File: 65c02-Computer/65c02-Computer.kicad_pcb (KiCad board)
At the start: 2 copper layers, 16 parts, among them SW1 SW_Push, U1 65C02, U2 62C256, U3 74LS04, U4 28C256, U5 LM555, X1 MXO-45HST

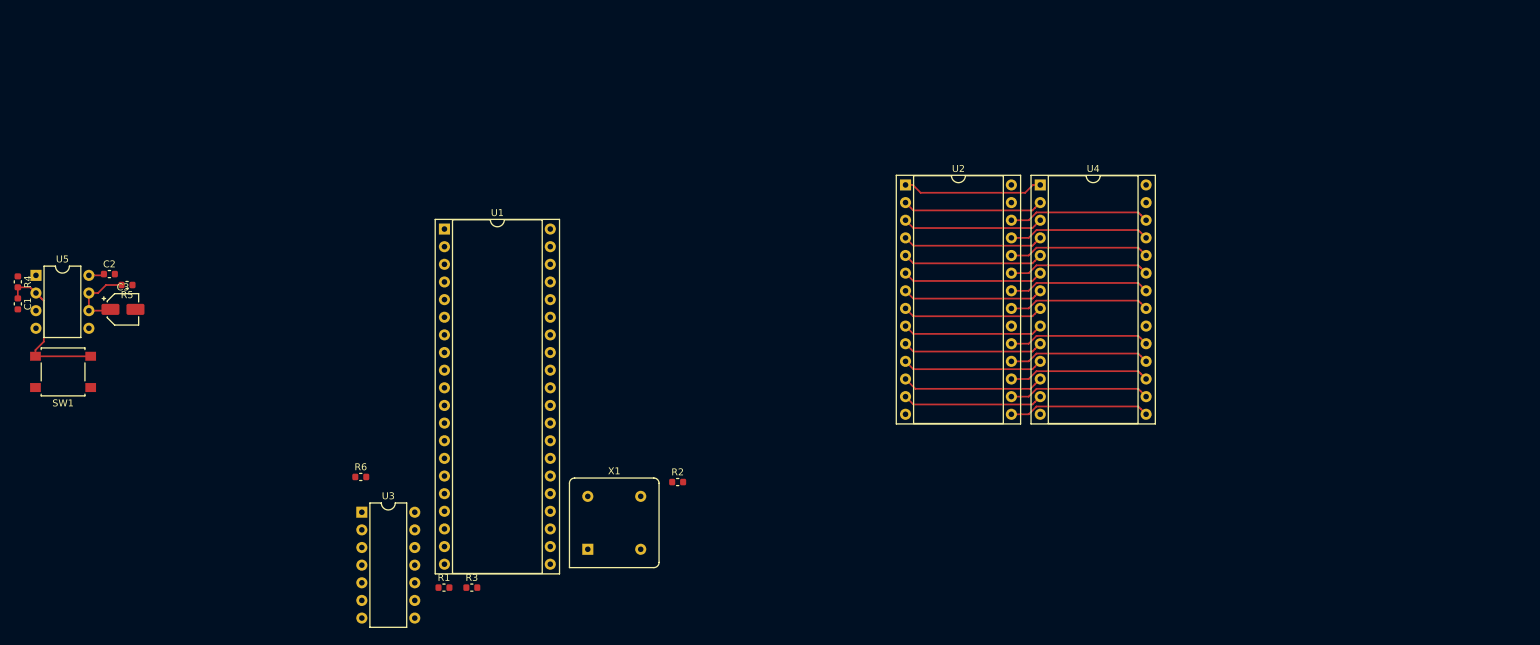
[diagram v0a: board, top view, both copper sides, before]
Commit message: Update pcb and put arduino sketch
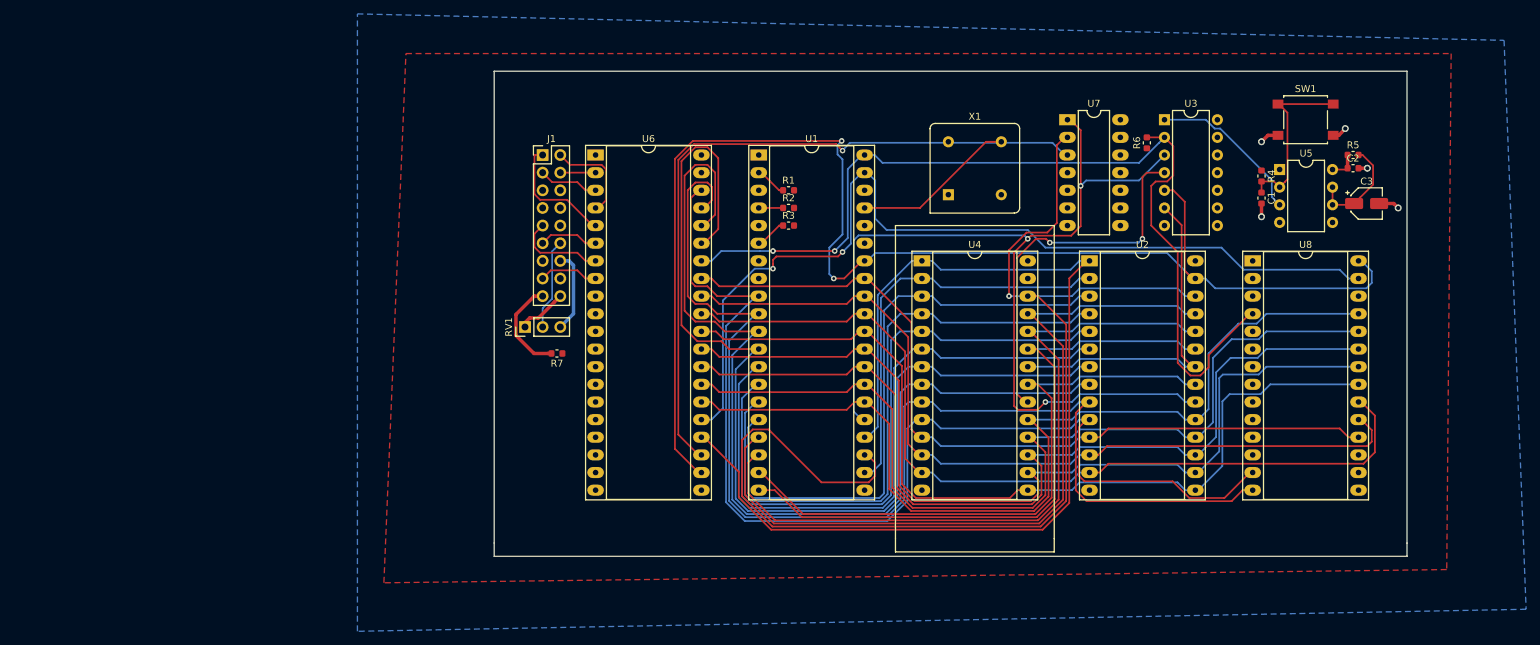
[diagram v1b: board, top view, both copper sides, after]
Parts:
- added J1: Conn_02x09_Odd_Even, Connector_PinHeader_2.54mm:PinHeader_2x09_P2.54mm_Vertical, F.Cu at (112.4, 38.1)
- added R7: 150, Resistor_SMD:R_0603_1608Metric, F.Cu at (114.5, 66.7)
- added RV1: 10k, Connector_PinHeader_2.54mm:PinHeader_1x03_P2.54mm_Vertical, F.Cu at (109.9, 62.9)
- added U6: 65C22, Package_DIP:DIP-40_W15.24mm_Socket_LongPads, F.Cu at (120.0, 38.1)
- added U7: 74LS32, Package_DIP:DIP-14_W7.62mm_LongPads, F.Cu at (188.0, 33.0)
- added U8: 65C51S, Package_DIP:DIP-28_W15.24mm_Socket_LongPads, F.Cu at (214.6, 53.3)
- U1: footprint Package_DIP:DIP-40_W15.24mm_Socket -> Package_DIP:DIP-40_W15.24mm_Socket_LongPads
- U2, U4: footprint Package_DIP:DIP-28_W15.24mm_Socket -> Package_DIP:DIP-28_W15.24mm_Socket_LongPads
- moved SW1 182.6 mm to (222.2, 33.0)
- moved C1 179.7 mm to (215.9, 44.3)
- moved C2 179.7 mm to (229.1, 40.0)
- moved C3 179.7 mm to (231.0, 45.1)
- moved R4 179.7 mm to (215.9, 41.1)
- moved U5 179.7 mm to (218.5, 40.2)
- moved R5 177.5 mm to (229.1, 38.1), turned to 0 degrees
- moved U3 128.6 mm to (201.9, 33.0)
- moved R6 123.0 mm to (199.4, 36.3), turned to 90 degrees
- moved R1 75.7 mm to (147.8, 43.2)
- moved X1 72.8 mm to (170.8, 43.8)
- moved R3 69.3 mm to (147.8, 48.3)
- moved U1 46.5 mm to (143.5, 38.1)
- moved R2 42.6 mm to (147.8, 45.7)
- moved U2 28.7 mm to (191.1, 53.3)
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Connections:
- net /Reset/~RESET renamed /~RESET
- net Net-(U1-Pad37) renamed /CLK
- U1 pad 39: (no net) -> /PHI2
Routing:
- net ~WR: track 0.00 -> 194.6 mm, vias 0 -> 2
- net /A13: track 20.3 -> 174.0 mm, vias 0 -> 1
- net /A1: track 20.3 -> 173.4 mm
- net /A15: track 0.00 -> 143.5 mm, vias 0 -> 3
- net /A0: track 20.3 -> 160.7 mm
- net /~RESET: track 0.00 -> 136.5 mm, vias 0 -> 2
- net /PHI2: track 0.00 -> 134.2 mm, vias 0 -> 2
- net /A14: track 20.3 -> 154.0 mm
- net /A3: track 20.3 -> 151.7 mm
- net /A2: track 20.3 -> 142.3 mm
- net /D7: track 20.3 -> 135.9 mm
- net /D6: track 20.3 -> 135.1 mm
- net /D5: track 20.3 -> 133.5 mm
- net /D4: track 20.3 -> 132.7 mm
- net /D3: track 20.3 -> 128.6 mm
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- added copper zone on F.Cu, net +5V
- added copper zone on B.Cu, net GND
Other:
- board outline added: 131.4 x 69.9 mm
- net class Power added: clearance 0.2, trace_width 0.5, via_dia 1, via_drill 0.6

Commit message: Create v2
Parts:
- removed the C2 at (229.1, 40.0)
- removed the R4 at (215.9, 41.1)
- removed the U5 at (218.5, 40.2)
- added C1: 27p, Capacitor_THT:C_Disc_D3.8mm_W2.6mm_P2.50mm, F.Cu at (213.4, 85.7)
- added C4: 10u, Capacitor_THT:CP_Radial_D8.0mm_P5.00mm, F.Cu at (231.0, 46.4)
- added J1: Barrel_Jack, Connector_BarrelJack:BarrelJack_CUI_PJ-102AH_Horizontal, F.Cu at (259.7, 41.3)
- added J2: Conn_01x06, Connector_PinSocket_2.54mm:PinSocket_1x06_P2.54mm_Horizontal, F.Cu at (250.2, 37.5)
- added J4: Conn_01x02, Connector_PinHeader_2.54mm:PinHeader_1x02_P2.54mm_Vertical, F.Cu at (229.2, 31.1)
- added R6: 30k, Resistor_THT:R_Axial_DIN0207_L6.3mm_D2.5mm_P10.16mm_Horizontal, F.Cu at (233.0, 30.5)
- added U10: 74LS138, Package_DIP:DIP-16_W7.62mm_LongPads, F.Cu at (189.2, 30.5)
- added U6: 65C22, Package_DIP:DIP-40_W15.24mm_Socket_LongPads, F.Cu at (89.5, 38.1)
- added U9: 74LS30, Package_DIP:DIP-14_W7.62mm_LongPads, F.Cu at (210.8, 53.3)
- added Y1: 1.8432MHz, Crystal:Crystal_HC49-U_Vertical, F.Cu at (214.6, 79.4)
- C2: renamed from C1; footprint Capacitor_SMD:C_0603_1608Metric -> Capacitor_THT:C_Disc_D3.8mm_W2.6mm_P2.50mm
- C3: value 10u -> C; footprint Capacitor_SMD:CP_Elec_4x3 -> Capacitor_THT:C_Disc_D3.8mm_W2.6mm_P2.50mm
- R1, R2, R3: footprint Resistor_SMD:R_0603_1608Metric -> Resistor_THT:R_Axial_DIN0207_L6.3mm_D2.5mm_P10.16mm_Horizontal
- R4: renamed from R7; footprint Resistor_SMD:R_0603_1608Metric -> Resistor_THT:R_Axial_DIN0207_L6.3mm_D2.5mm_P10.16mm_Horizontal
- R5: value 30k -> 1M; footprint Resistor_SMD:R_0603_1608Metric -> Resistor_THT:R_Axial_DIN0207_L6.3mm_D2.5mm_P10.16mm_Horizontal
- R7: renamed from R6; footprint Resistor_SMD:R_0603_1608Metric -> Resistor_THT:R_Axial_DIN0207_L6.3mm_D2.5mm_P10.16mm_Horizontal
- SW1: footprint Button_Switch_SMD:SW_SPST_B3S-1000 -> Button_Switch_THT:SW_PUSH_6mm_H4.3mm
- U7: value 74LS32 -> LM555; footprint Package_DIP:DIP-14_W7.62mm_LongPads -> Package_DIP:DIP-8_W7.62mm
- moved U7 31.4 mm to (218.5, 40.2)
- moved R5 16.4 mm to (215.3, 29.2), turned to 270 degrees
- moved R7 13.5 mm to (210.8, 29.2), turned to 180 degrees
- moved R2 9.56 mm to (139.7, 40.6), turned to 90 degrees
- moved R4 9.54 mm to (114.9, 76.2), turned to 90 degrees
- moved R3 9.24 mm to (139.7, 43.8), turned to 270 degrees
- moved R1 9.06 mm to (146.1, 34.3)
- moved U2 8.25 mm to (222.9, 53.3)
- moved C3 5.39 mm to (229.2, 40.0), turned to 90 degrees
- moved SW1 4.07 mm to (225.4, 35.6)
- moved C2 1.86 mm to (215.3, 42.5)
- renumbered J1 to J3, U8 to U2, U2 to U3, U6 to U5, U3 to U8
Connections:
- C2 pad 1: Net-(C1-Pad1) -> Net-(C2-Pad1)
- C3 pad 1: Net-(C3-Pad1) -> +5V
- R5 pad 2: Net-(C3-Pad1) -> Net-(C2-Pad1)
- SW1 pad 2: Net-(C1-Pad1) -> Net-(C2-Pad1)
- U2 pad 10: (no net) -> Net-(J2-Pad2)
- U2 pad 12: (no net) -> Net-(J2-Pad3)
- U2 pad 16: (no net) -> GND
- U2 pad 17: (no net) -> GND
- U2 pad 2: (no net) -> +5V
- U2 pad 3: (no net) -> /ACIA_CS1B
- U2 pad 6: (no net) -> Net-(U2-Pad6)
- U2 pad 7: (no net) -> Net-(C1-Pad1)
- U2 pad 9: (no net) -> GND
- U5 pad 24: /A14 -> +5V
- U7 pad 1: /A15 -> GND
- U7 pad 2: /A13 -> Net-(C2-Pad1)
- U7 pad 3: /V1_CS2B -> Net-(U7-Pad3)
- U7 pad 4: (no net) -> +5V
- U7 pad 6: (no net) -> Net-(C4-Pad1)
- U7 pad 7: (no net) -> Net-(C4-Pad1)
- U7 pad 8: (no net) -> +5V
- U8 pad 1: Net-(U3-Pad1) -> Net-(U7-Pad3)
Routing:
- net /V2_CS2B: track 0.00 -> 136.9 mm
- net GND: track 18.4 -> 99.4 mm, vias 5 -> 8
- net Net-(J2-Pad3): track 0.00 -> 61.6 mm, vias 0 -> 1
- net Net-(J2-Pad2): track 0.00 -> 60.0 mm, vias 0 -> 1
- net Net-(U10-Pad5): track 0.00 -> 49.9 mm
- net /D3: track 128.6 -> 176.9 mm
- net /A2: track 142.3 -> 187.4 mm, vias 0 -> 2
- net ~WR: track 194.6 -> 238.9 mm
- net /D4: track 132.7 -> 176.5 mm
- net /A0: track 160.7 -> 203.3 mm, vias 0 -> 2
- net /A1: track 173.4 -> 215.6 mm, vias 0 -> 2
- net /D0: track 116.1 -> 157.3 mm
- net /D5: track 133.5 -> 174.1 mm, vias 0 -> 1
- net /D1: track 124.5 -> 164.5 mm
- net /ACIA_CS1B: track 0.00 -> 40.0 mm, vias 0 -> 1
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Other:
- board size 131.4 x 69.9 mm -> 186.7 x 69.9 mm
